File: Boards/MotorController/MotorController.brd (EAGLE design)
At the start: 43.2 x 58.4 mm, 21 parts, among them IC1 MC33926

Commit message: Modifying motor controller
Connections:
- removed net PWM: APM.9, IC1.2
- new net PWM1: APM.8, IC1.2
- new net PWM2: APM.9, IC1.1
- net GND: no longer IC1.1
- net INV: now also APM.7; no longer APM.8
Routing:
- net PWM: track 8.28 -> 0.00 mm, vias 1 -> 0
- net PWM1: track 0.00 -> 6.52 mm, vias 0 -> 1
- net INV: track 17.7 -> 14.9 mm
- net GND: track 65.1 -> 62.7 mm
- net FB: track 57.2 -> 57.7 mm

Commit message: Rev B Motor Controller
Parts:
- added U$7: 5PIN5PIN_MC, pie:5PIN_MC
- moved U$4 33.5 mm to (38.8, 11.7)
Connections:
- net GND: now also CONN2.PIN2, U$7.GND; no longer CONN2.PIN1
- net INV: now also U$7.INV
- net OUT1: now also CONN1.PIN1; no longer CONN1.PIN2
- net OUT2: now also CONN1.PIN2; no longer CONN1.PIN1
- net PWM1: now also U$7.PWM1
- net PWM2: now also U$7.PWM2
- net VCC: now also U$7.VCC
- net VPWR: now also CONN2.PIN1; no longer CONN2.PIN2
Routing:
- net PWM1: track 6.52 -> 27.1 mm
- net VCC: track 78.9 -> 98.7 mm, vias 3 -> 4
- net PWM2: track 0.00 -> 19.0 mm, vias 0 -> 1
- net INV: track 14.9 -> 33.5 mm
- net VPWR: track 75.3 -> 83.1 mm
- net OUT1: track 39.3 -> 33.0 mm
- net OUT2: track 20.1 -> 26.4 mm
- net GND: track 62.7 -> 60.8 mm
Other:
- board text added: "MotorController Rev B"
- board text removed: "MotorController Prototype"

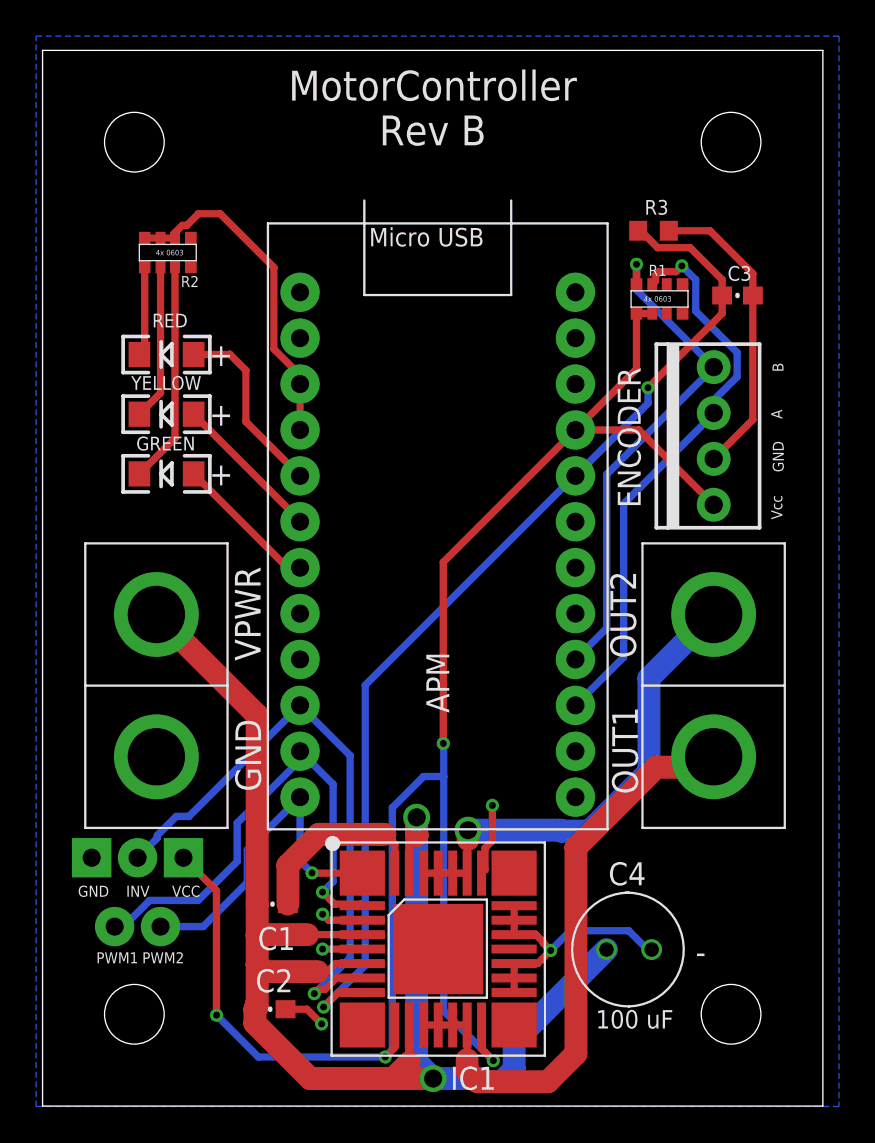
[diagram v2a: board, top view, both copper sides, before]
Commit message: Fixed routing to arduino pins
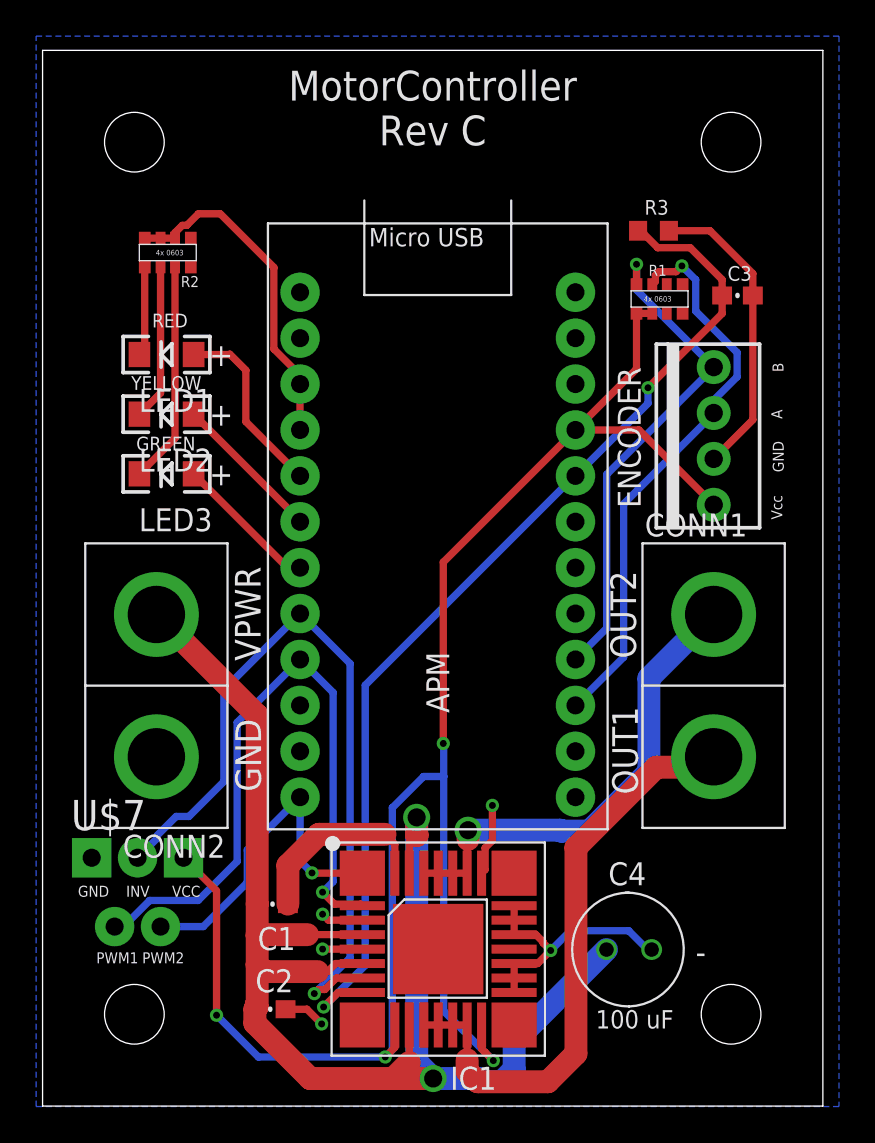
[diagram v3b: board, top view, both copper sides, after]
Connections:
- net INV: now also APM.5; no longer APM.7
- net PWM1: now also APM.6; no longer APM.8
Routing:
- net PWM1: track 27.1 -> 37.3 mm
- net INV: track 33.5 -> 43.7 mm
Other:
- board text added: "MotorController Rev C"
- board text removed: "MotorController Rev B"
